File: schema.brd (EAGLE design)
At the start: 31.4 x 38.1 mm, 7 parts, among them X1 BU-SMA-G

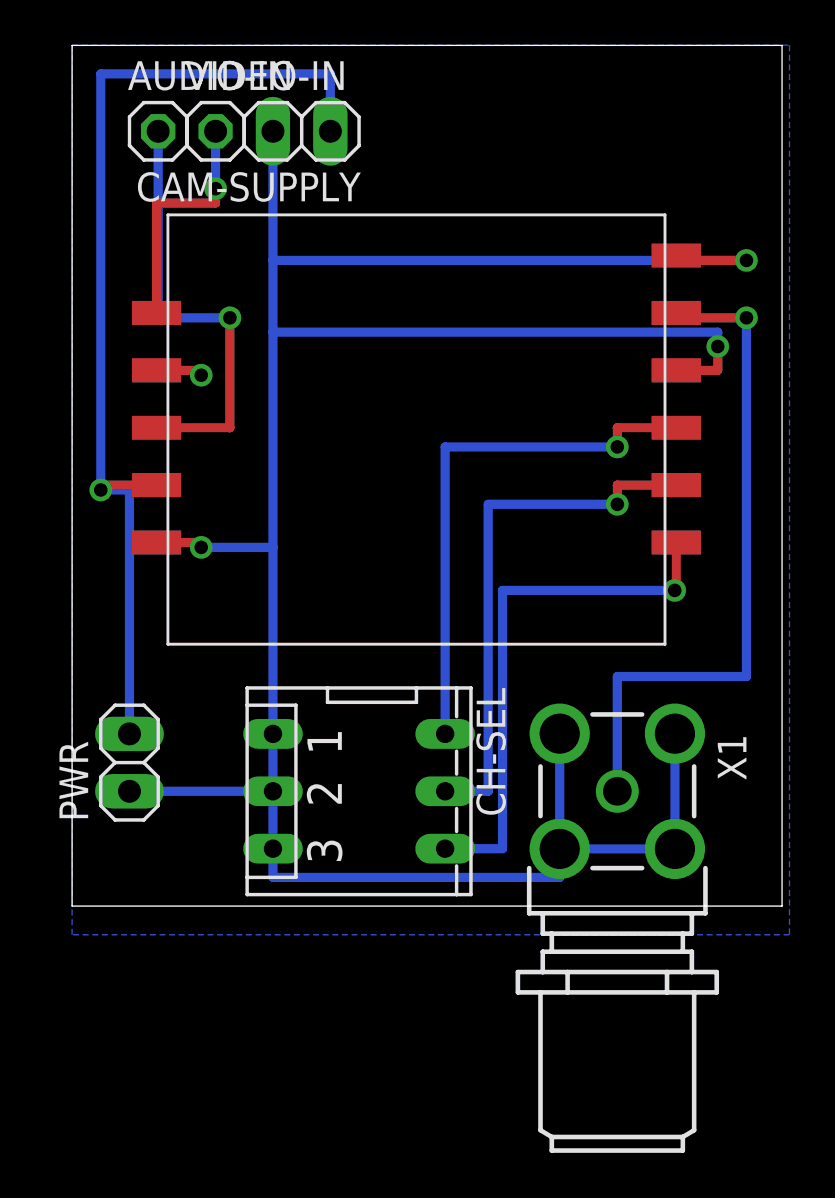
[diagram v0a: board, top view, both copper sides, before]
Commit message: Pin swap issue on FX758 fixed
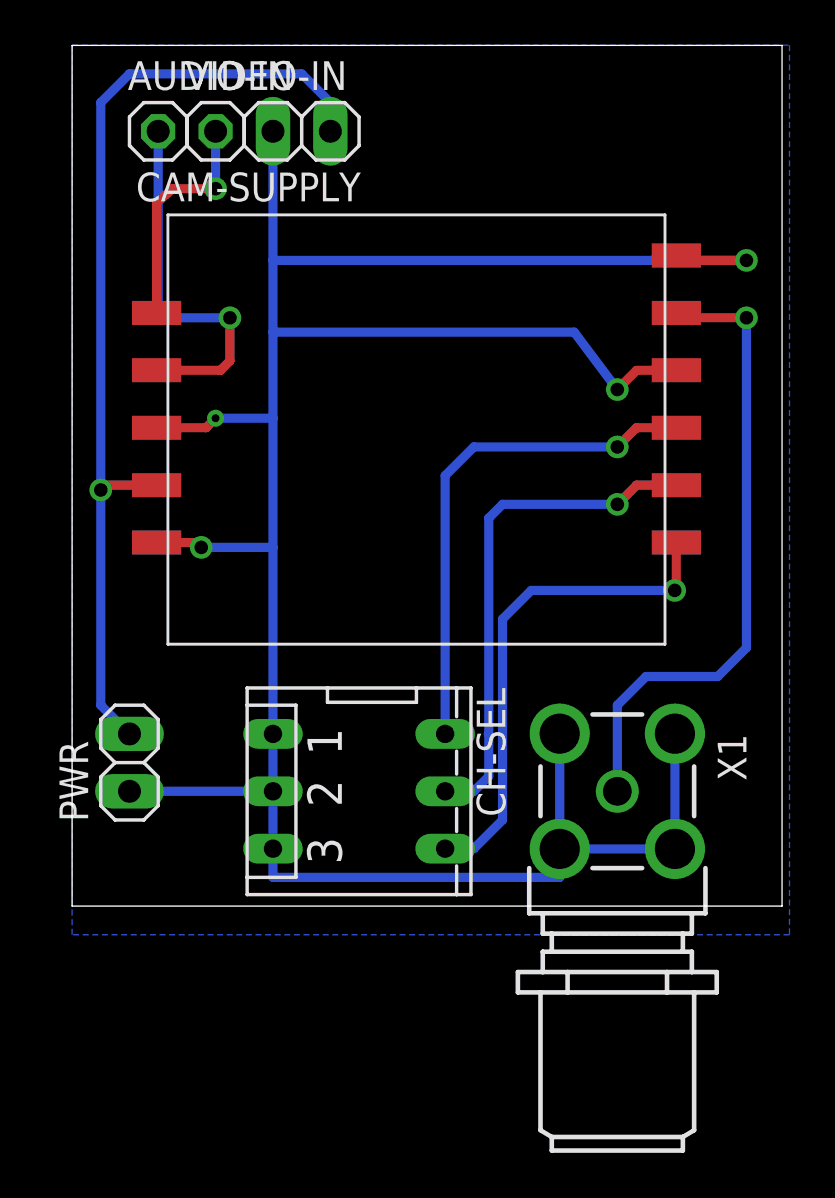
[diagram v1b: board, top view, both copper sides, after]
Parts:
- TRANSMITTER: device hi-link:FX758 -> custom-parts:FX758
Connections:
- net AUDIO-IN: now also TRANSMITTER.P$3; no longer TRANSMITTER.P$4
- net GND: now also TRANSMITTER.P$4; no longer TRANSMITTER.P$3
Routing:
- net AUDIO-IN: track 19.5 -> 16.4 mm
- net +5V: track 45.9 -> 43.5 mm
- net ANTENA: track 30.8 -> 29.0 mm
- net CH1: track 23.8 -> 22.3 mm
- net CH3: track 23.8 -> 22.5 mm
- net CH2: track 23.8 -> 22.6 mm
- net GND: track 123.5 -> 122.8 mm

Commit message: Minor adjustments
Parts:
- AUDIO-IN: value (none) -> A
- CAM-SUPPLY, PWR: value (none) -> G 5V
- VIDEO-IN: value (none) -> V
- renumbered X1 to SMA
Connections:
- net CH1: now also CH-SEL.1; no longer CH-SEL.4
- net CH2: now also CH-SEL.2; no longer CH-SEL.5
- net CH3: now also CH-SEL.3; no longer CH-SEL.6
- net GND: now also CH-SEL.4, CH-SEL.5, CH-SEL.6; no longer CH-SEL.1, CH-SEL.2, CH-SEL.3
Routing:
- net CH3: track 22.5 -> 37.1 mm
- net GND: track 122.8 -> 111.3 mm
- net CH2: track 22.6 -> 31.8 mm
- net CH1: track 22.3 -> 26.0 mm
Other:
- board text added: "FX758"
- board text added: "rev. 2.0 May-2017"
